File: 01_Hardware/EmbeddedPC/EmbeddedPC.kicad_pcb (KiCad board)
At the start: 2 copper layers, 2 parts, among them U2 AP7370

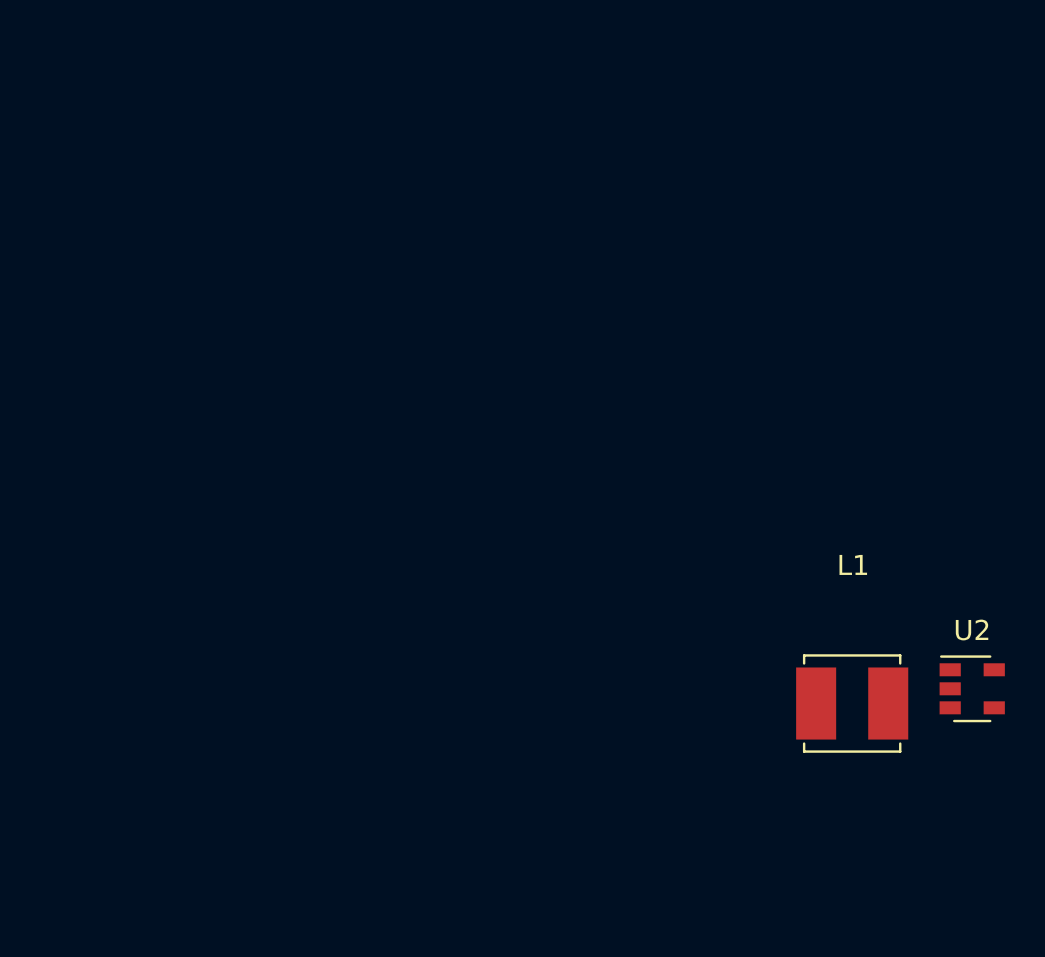
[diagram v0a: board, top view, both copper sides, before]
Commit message: update layout: - RAM - MCU - FLASH
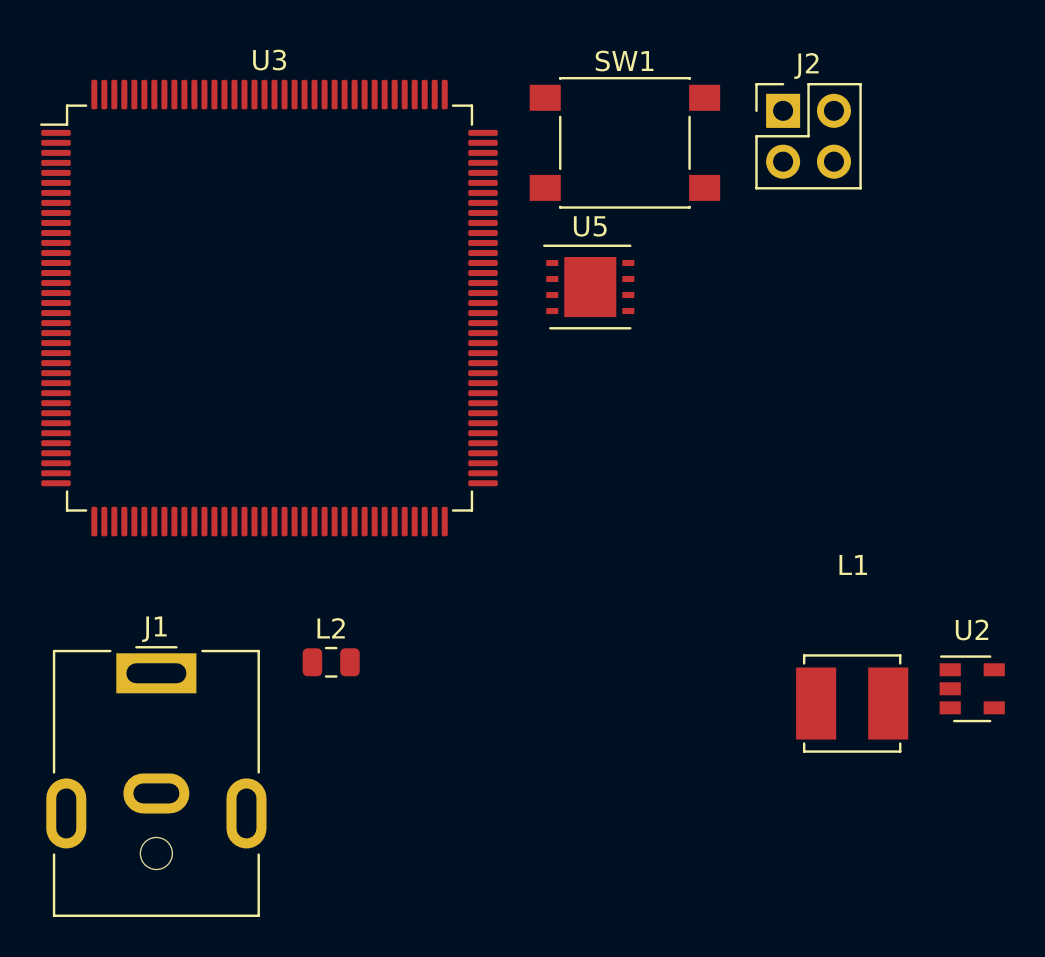
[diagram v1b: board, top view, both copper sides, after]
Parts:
- added J1: Jack-DC, Connector_BarrelJack:BarrelJack_CUI_PJ-063AH_Horizontal, F.Cu at (91.5, -5.70)
- added J2: RPG, Connector_PinHeader_2.54mm:PinHeader_2x02_P2.54mm_Vertical, F.Cu at (122.8, -33.8)
- added L2: 10uH, Capacitor_SMD:C_0805_2012Metric, F.Cu at (100.2, -6.25)
- added SW1: SW_Push, Button_Switch_SMD:SW_SPST_PTS645, F.Cu at (114.8, -32.2)
- added U3: STM32H743ZITx, Package_QFP:LQFP-144_20x20mm_P0.5mm, F.Cu at (97.1, -23.9)
- added U5: TH58CVG3S0HRAIJ, Package_SON:WSON-8_4x4mm_P0.8mm, F.Cu at (113.1, -25.0)
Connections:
- U2 pad 2: Net-(U2-Pad2) -> GND
- U2 pad 3: Net-(U2-Pad3) -> (no net)
- U2 pad 4: Net-(U2-Pad4) -> (no net)
- U2 pad 5: Net-(U2-Pad5) -> +3V3
